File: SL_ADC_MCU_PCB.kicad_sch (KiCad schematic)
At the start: 20 parts, among them IC1 ADS8528SPM

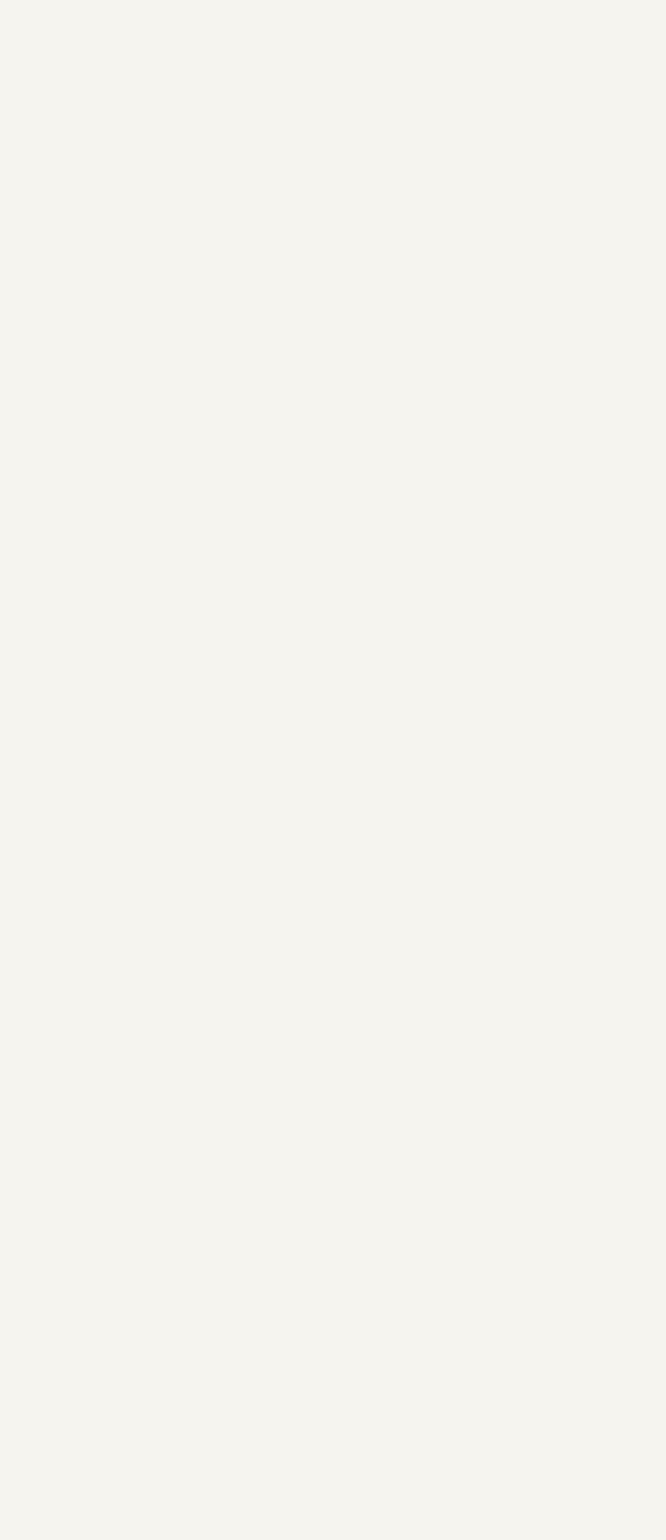
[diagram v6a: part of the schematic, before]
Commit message: madded a 0 ohm resistor
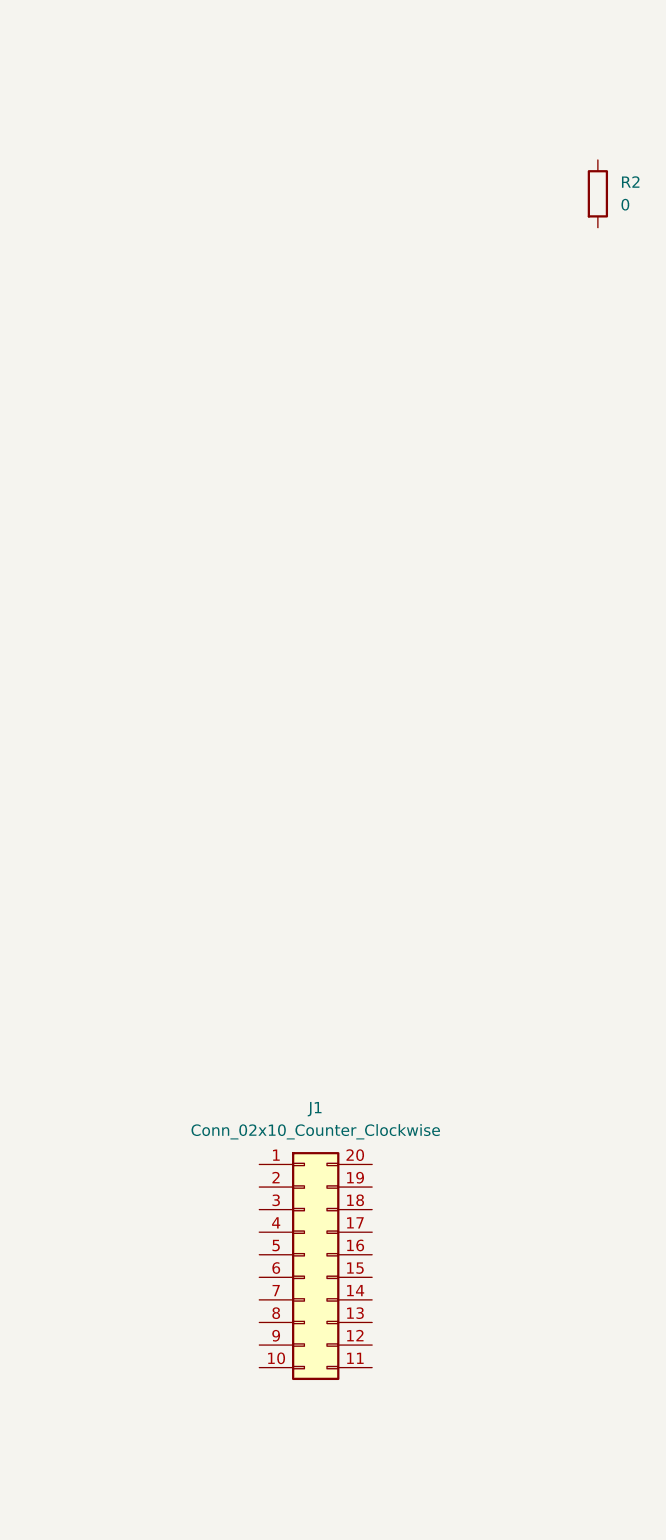
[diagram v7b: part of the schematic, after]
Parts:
- added J1: Conn_02x10_Counter_Clockwise, symbol Connector_Generic:Conn_02x10_Counter_Clockwise
- added R2: 0, Resistor_SMD:R_0805_2012Metric_Pad1.20x1.40mm_HandSolder, symbol Device:R
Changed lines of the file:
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@@
+	)
+	(symbol
+		(lib_id "Connector_Generic:Conn_02x10_Counter_Clockwise")
+		(at 384.81 212.09 0)
+		(unit 1)
+		(exclude_from_sim no)
+		(in_bom yes)
+		(on_board yes)
+		(dnp no)
+		(fields_autoplaced yes)
+		(property "Reference" "J1"
+			(at 386.08 195.58 0)
+			(effects
+				(font
+					(size 1.27 1.27)
+				)
+			)
+		)
+		(property "Value" "Conn_02x10_Counter_Clockwise"
+			(at 386.08 198.12 0)
+			(effects
+				(font
+					(size 1.27 1.27)
+				)
+			)
+		)
+		(property "Footprint" ""
+			(at 384.81 212.09 0)
+			(effects
+				(font
+					(size 1.27 1.27)
+				)
+				(hide yes)
+			)
+		)
+		(property "Datasheet" "~"
+			(at 384.81 212.09 0)
+			(effects
+				(font
+					(size 1.27 1.27)
+				)
+				(hide yes)
+			)
+		)
+		(property "Description" "Generic connector, double row, 02x10, counter clockwise pin numbering scheme (similar to DIP package numbering), script generated (kicad-library-utils/schlib/autogen/connector/)"
+			(at 384.81 212.09 0)
+			(effects
+				(font
+					(size 1.27 1.27)
+				)
+				(hide yes)
+			)
+		)
+		(pin "4"
+		)
+		(pin "10"
+		)
+		(pin "19"
+		)
+		(pin "2"
+		)
+		(pin "3"
+		)
+		(pin "5"
+		)
+		(pin "8"
+		)
+		(pin "9"
+		)
+		(pin "6"
+		)
+		(pin "1"
+		)
+		(pin "7"
+		)
+		(pin "20"
+		)
+		(pin "13"
+		)
+		(pin "17"
+		)
+		(pin "11"
+		)
+		(pin "16"
+		)
+		(pin "14"
+		)
+		(pin "18"
+		)
+		(pin "12"
+		)
+		(pin "15"
+		)
+		(instances
+			(project ""
+				(path "/3f4eb23c-7a54-403d-a4d1-8d06ed1540f4"
+					(reference "J1")
+					(unit 1)
+				)
+			)
+		)
 	)
 	(symbol
@@
 					(unit 1)
 				)
+			)
+		)
+	)
+	(symbol
+		(lib_id "Device:R")
+		(at 417.83 92.71 0)
+		(unit 1)
+		(exclude_from_sim no)
+		(in_bom yes)
+		(on_board yes)
+		(dnp no)
+		(fields_autoplaced yes)
+		(property "Reference" "R2"
+			(at 420.37 91.4399 0)
+			(effects
+				(font
+					(size 1.27 1.27)
+				)
+				(justify left)
+			)
+		)
+		(property "Value" "0"
+			(at 420.37 93.9799 0)
+			(effects
+				(font
+					(size 1.27 1.27)
+				)
+				(justify left)
+			)
+		)
+		(property "Footprint" "Resistor_SMD:R_0805_2012Metric_Pad1.20x1.40mm_HandSolder"
+			(at 416.052 92.71 90)
+			(effects
+				(font
+					(size 1.27 1.27)
+				)
+				(hide yes)
+			)
+		)
+		(property "Datasheet" "~"
+			(at 417.83 92.71 0)
+			(effects
+				(font
+					(size 1.27 1.27)
+				)
+				(hide yes)
+			)
+		)
+		(property "Description" "Resistor"
+			(at 417.83 92.71 0)
+			(effects
+				(font
+					(size 1.27 1.27)
+				)
+				(hide yes)
+			)
+		)
+		(property "Manufacturer_Part_Number" "RC0805JR-070RL"
+			(at 417.83 92.71 0)
+			(effects
+				(font
+					(size 1.27 1.27)
+				)
+				(hide yes)
+			)
+		)
+		(pin "1"
+		)
+		(pin "2"
+		)
+		(instances
+			(project ""
+				(path "/3f4eb23c-7a54-403d-a4d1-8d06ed1540f4"
+					(reference "R2")
+					(unit 1)
+				)

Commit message: 0-ohm resistor for mcu power and added header for power and hydrophone channels
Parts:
- removed J1: Conn_02x10_Counter_Clockwise, symbol Connector_Generic:Conn_02x10_Counter_Clockwise
- added J1: Conn_02x14_Counter_Clockwise, Connector_PinHeader_2.54mm:PinHeader_2x14_P2.54mm_Vertical, symbol Connector_Generic:Conn_02x14_Counter_Clockwise
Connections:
- net DGND is gone; now on net AGND: C18.2, IC1.24 (DGND)
- net -5V-HVSS: now also J1.26 (Pin_26), J1.3 (Pin_3)
- net 5V-HVDD: now also J1.2 (Pin_2), J1.27 (Pin_27)
- net AGND: now also J1.23 (Pin_23), J1.24 (Pin_24), J1.5 (Pin_5), J1.6 (Pin_6)
- net AVDD: now also R2.1, J1.1 (Pin_1), J1.28 (Pin_28)
- net CH_A0: now also J1.22 (Pin_22), J1.7 (Pin_7)
- net CH_A1: now also J1.21 (Pin_21), J1.8 (Pin_8)
- net CH_B0: now also J1.20 (Pin_20), J1.9 (Pin_9)
- net CH_B1: now also J1.10 (Pin_10), J1.19 (Pin_19)
- net CH_C0: now also J1.11 (Pin_11), J1.18 (Pin_18)
- net CH_C1: now also J1.12 (Pin_12), J1.17 (Pin_17)
- net CH_D0: now also J1.13 (Pin_13), J1.16 (Pin_16)
- net CH_D1: now also J1.14 (Pin_14), J1.15 (Pin_15)
- net DVDD: now also STM1.3V31, J1.25 (Pin_25), J1.4 (Pin_4)
- net 5V1: now reaches STM1.5V1
- net 5V1: now also R2.2
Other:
- moved on the sheet: R2
